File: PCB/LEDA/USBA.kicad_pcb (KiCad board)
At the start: 2 copper layers, 70 x 70 mm, 24 parts, among them J1 USB_A, J2 Conn_01x03, T1 T3902_MEMS_Mic, U1 VEML6040, U2 ESP32-S3-MINI-1, U5 MD8942

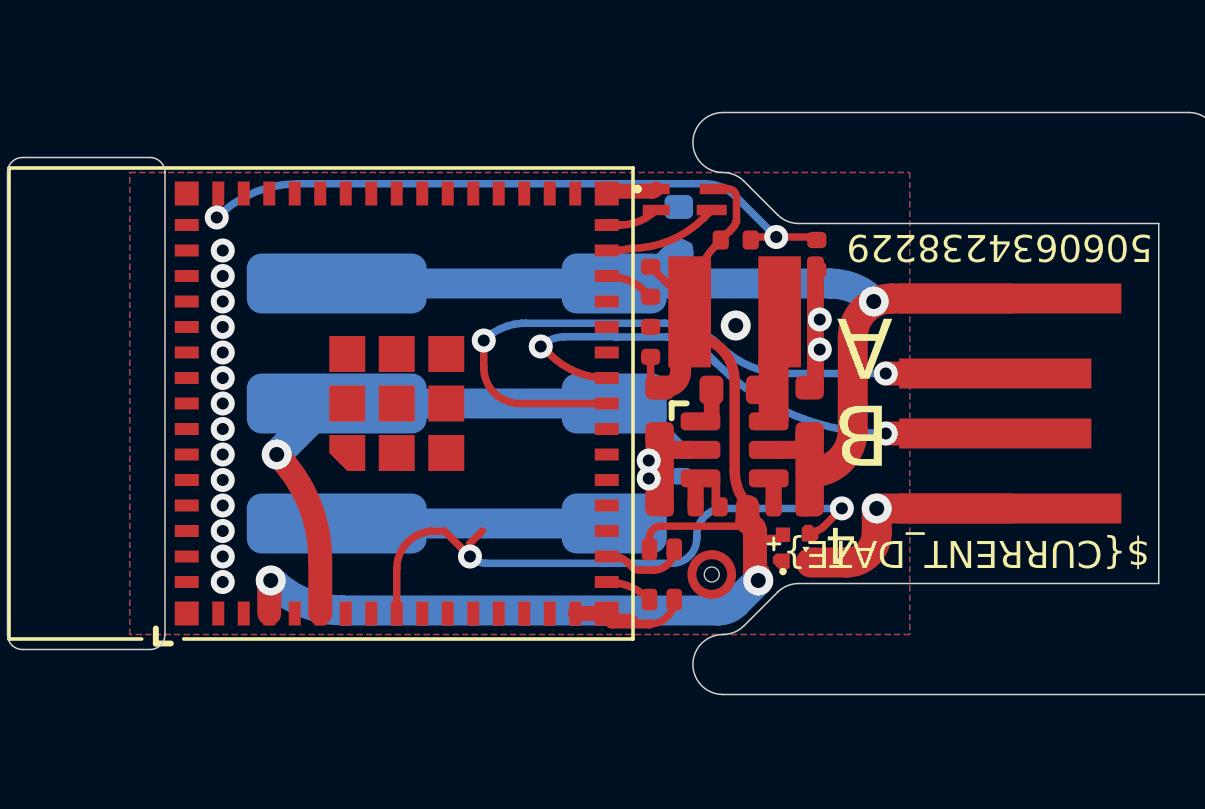
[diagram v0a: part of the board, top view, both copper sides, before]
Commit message: Retrack to move USB away from power
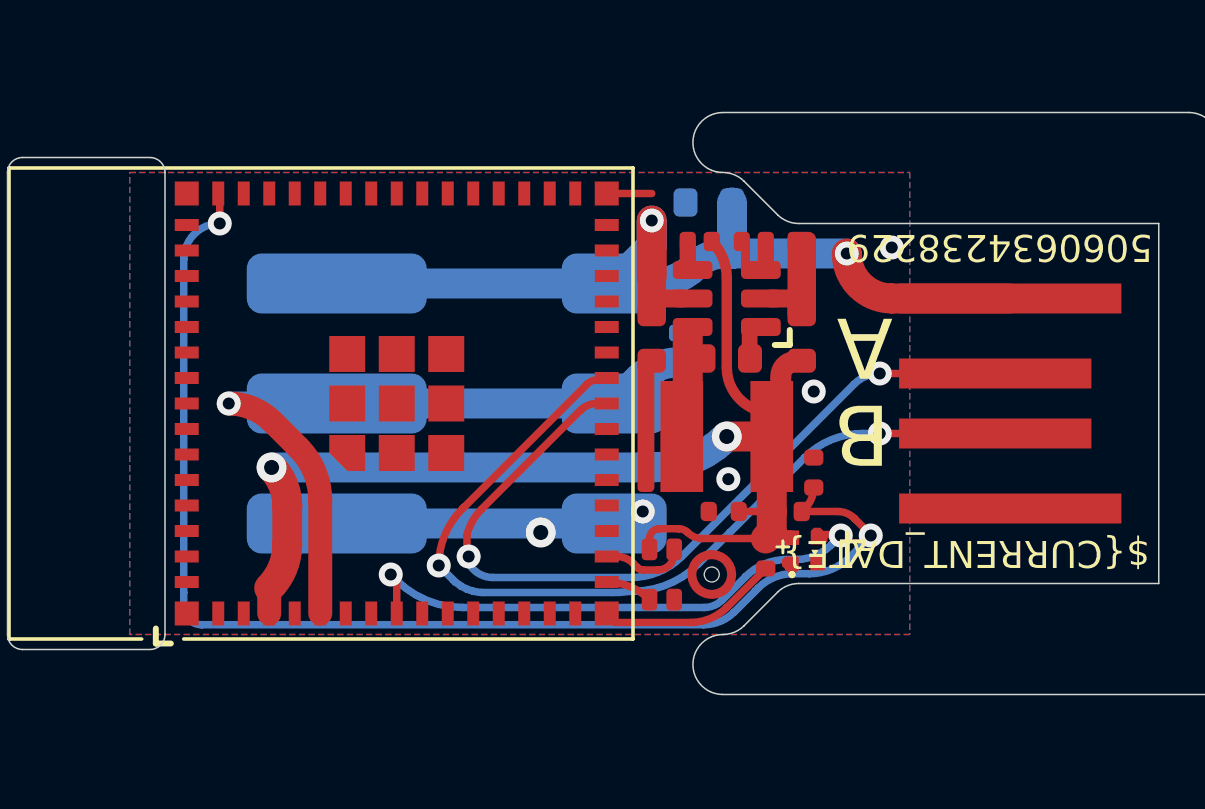
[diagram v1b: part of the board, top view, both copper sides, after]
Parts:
- removed U1: VEML6040, RevK:VEML6040
- moved C2 9.83 mm to (107.9, 104.3)
- moved R11 9.65 mm to (104.8, 93.9), turned to 0 degrees
- moved R10 9.45 mm to (108.4, 93.9), turned to 0 degrees
- moved R1 9.21 mm to (108.6, 102.9)
- moved R9 8.85 mm to (106.6, 93.9), turned to 0 degrees
- moved C3 7.25 mm to (109.5, 101.6), turned to 90 degrees
- moved C1 6.16 mm to (106.5, 102.9), turned to 180 degrees
- moved C6 5.80 mm to (104.1, 97.1), turned to 90 degrees
- moved C7 5.33 mm to (109.1, 97.1), turned to -90 degrees
- moved U5 5.05 mm to (106.6, 95.8), turned to 0 degrees
- moved L2 4.16 mm to (106.6, 100.4), turned to 0 degrees
- moved D2 3.93 mm to (105.0, 97.4), turned to -90 degrees
- moved C4 1.36 mm to (106.0, 92.6), turned to 180 degrees
- moved C8 1.08 mm to (106.6, 97.8), turned to 0 degrees
- moved D1 0.32 mm to (109.2, 104.2)
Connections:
- U2 pad 15: GND -> unconnected-(U2-GPIO11-Pad15)
- U2 pad 20: GND -> unconnected-(U2-GPIO16-Pad20)
- U2 pad 21: GND -> unconnected-(U2-GPIO17-Pad21)
- U2 pad 22: GND -> unconnected-(U2-GPIO18-Pad22)
- U2 pad 28: GND -> unconnected-(U2-GPIO33-Pad28)
- U2 pad 29: SCL -> unconnected-(U2-GPIO34-Pad29)
- U2 pad 30: SDA -> unconnected-(U2-GPIO48-Pad30)
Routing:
- net Net-(U2-EN): track 22.8 -> 42.2 mm
- net D+: track 18.6 -> 29.4 mm
- net GND: track 24.4 -> 16.8 mm, vias 20 -> 5
- net D-: track 23.3 -> 27.9 mm
- net SCL: track 3.67 -> 0.00 mm
- net LED2: track 20.4 -> 24.0 mm
- net LED1: track 20.8 -> 18.1 mm
- net +3.3V: track 34.4 -> 31.9 mm
- net SDA: track 1.78 -> 0.00 mm
- net VBUS: track 31.1 -> 29.7 mm, vias 1 -> 2
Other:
- board text removed: "SDA:48 SCL:34"

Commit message: LEFT
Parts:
- moved C2 3.65 mm to (104.5, 103.1), turned to 0 degrees
- moved T1 0.30 mm to (105.3, 105.3)
- moved R1 0.24 mm to (108.4, 102.8)
- moved C1 0.10 mm to (106.5, 102.8)
- moved D1 0.10 mm to (109.2, 104.1)
- moved C3 0.10 mm to (109.5, 101.5)
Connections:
- T1 pad 2: GND -> +3.3V
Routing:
- net +3.3V: track 31.9 -> 39.0 mm
- net GND: track 16.8 -> 10.8 mm, vias 5 -> 6
- net VBUS: track 29.7 -> 28.5 mm

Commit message: SS
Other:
- board text added: "PDM:L"

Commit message: New mic
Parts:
- removed T1: T3902_MEMS_Mic, RevK:T3902_MEMS_Mic
- added U1: ICS43434_MEMS_Mic, RevK:ICS43434_MEMS_Mic, F.Cu at (105.3, 105.1)
- moved C2 0.39 mm to (104.7, 102.8), turned to 180 degrees
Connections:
- U2 pad 16: DATA -> WS
- U2 pad 17: CLK -> SD
- U2 pad 18: unconnected-(U2-GPIO14-Pad18) -> +3.3V
- U2 pad 19: unconnected-(U2-GPIO15-Pad19) -> SCK
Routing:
- net +3.3V: track 39.0 -> 35.2 mm, vias 2 -> 3
- net SCK: track 0.00 -> 3.01 mm
- net CLK: track 2.88 -> 0.00 mm
- net DATA: track 1.69 -> 0.00 mm
- net WS: track 0.00 -> 1.66 mm
- net SD: track 0.00 -> 1.61 mm
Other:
- board text added: "C15 D13 W12"
- board text removed: "CLK:13 DAT:12"
- board text removed: "PDM:L"

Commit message: ADC and tidy SS
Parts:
- added R2: 124K, RevK:R_0402, B.Cu at (102.6, 92.7)
- added R3: 10K, RevK:R_0402, B.Cu at (100.8, 92.7)
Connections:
- net VBUS renamed DC
- U2 pad 9: unconnected-(U2-GPIO5-Pad9) -> ADC
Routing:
- net ADC: track 0.00 -> 15.9 mm, vias 0 -> 1
- net DC: track 28.5 -> 29.7 mm
- net GND: vias 6 -> 9
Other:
- board text added: "5"

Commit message: Rework
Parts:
- added ?: , , F.Cu at (119.4, 94.9)
- added ?: , , F.Cu at (116.3, 94.3)
- added J3: TC2030-USB-NL-DS, RevK:Tag-Connect_TC2030-IDC-NL_2x03_P1.27mm_Vertical, B.Cu at (119.1, 102.5)
- moved C1 0.70 mm to (106.5, 103.5)
- moved C2 0.70 mm to (104.7, 103.5)
- moved C3 0.70 mm to (109.5, 102.2)
- moved C4 0.70 mm to (106.0, 93.3)
- moved C6 0.70 mm to (104.1, 97.8)
- moved C7 0.70 mm to (109.1, 97.8)
- moved C8 0.70 mm to (106.6, 98.5)
- moved D1 0.70 mm to (109.2, 104.8)
- moved D2 0.70 mm to (105.0, 98.1)
- moved J1 0.70 mm to (121.0, 100.0)
- moved J2 0.70 mm to (98.2, 100.0)
- moved R1 0.70 mm to (108.4, 103.5)
- moved R2 0.70 mm to (102.6, 93.4)
- moved R3 0.70 mm to (100.8, 93.4)
- moved REF** 0.70 mm to (95.6, 100.0)
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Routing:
- net DC: track 29.7 -> 46.2 mm, vias 2 -> 3
- net D-: track 27.9 -> 36.3 mm, vias 2 -> 3
- net D+: track 29.2 -> 36.3 mm
- net Net-(U2-EN): track 42.7 -> 43.8 mm
- net LED1: track 18.1 -> 18.8 mm
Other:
- board text added: "-HERE-"
- board text added: "Glue tab"
- board text removed: "5060634238229"
- board text removed: "[Glue tab here]"

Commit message: Tryign to do extra holes
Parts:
- removed the ? at (119.4, 94.9)
- removed the ? at (116.3, 94.3)
- added ?: , clipboard:8abff937-711c-455e-bc8a-c75c5e04b52f, F.Cu at (120.1, 94.9)
